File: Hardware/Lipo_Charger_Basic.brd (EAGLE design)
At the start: 29.2 x 10.2 mm, 14 parts, among them U1 MCP73831, X1 Micro USB

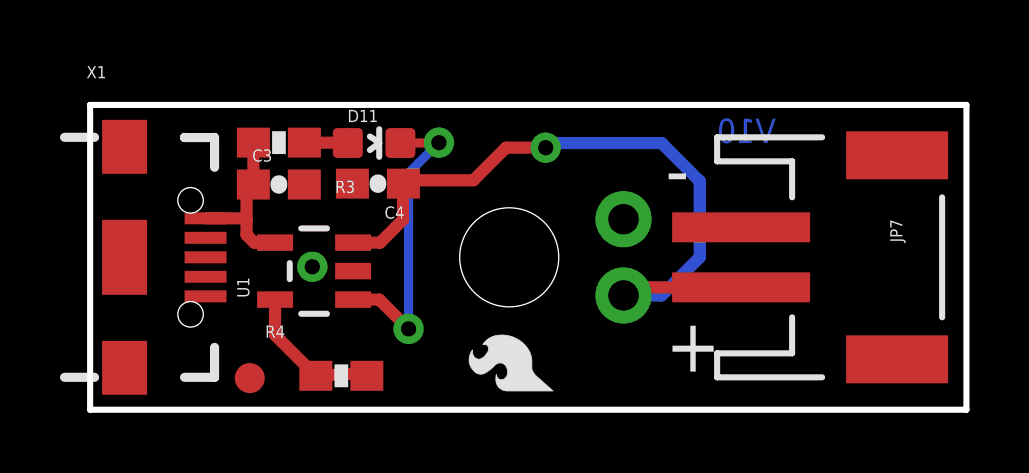
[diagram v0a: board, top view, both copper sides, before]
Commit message: Fixed sch and moved micro B
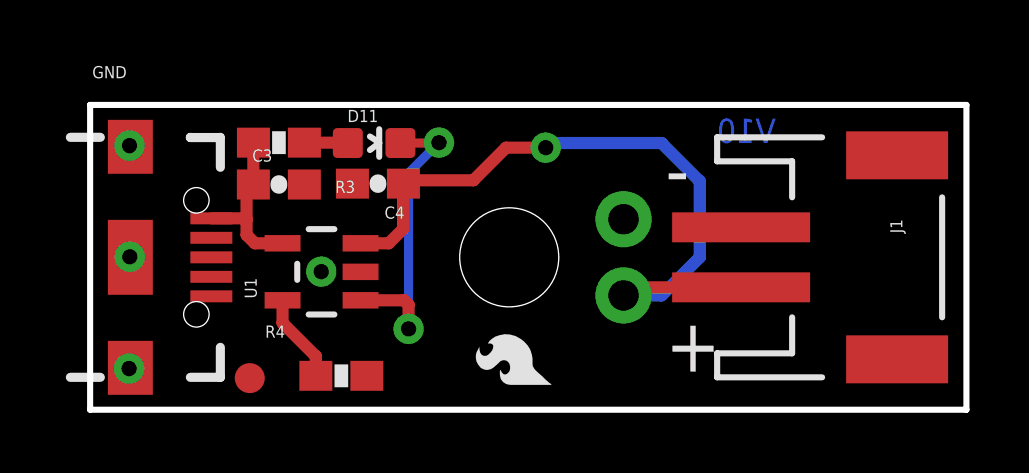
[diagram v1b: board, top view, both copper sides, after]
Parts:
- removed JP1: LOGO-SFESK, SparkFun:SFE-LOGO-FLAME
- removed JP7: LiPo Battery, SparkFun:JST-2-SMD
- removed X1: Micro USB, SparkFun-Connectors:USB-AB-MICRO-SMD_V03
- added GND: Micro USB, SparkFun-Connectors:USB-AB-MICRO-SMD_V03
- added J1: (no value), SparkFun-Connectors:JST-2-SMD
- added LOGO2: SFE_LOGO_FLAME.1_INCH, SparkFun-Aesthetics:SFE_LOGO_FLAME_.1
- JP8: value (none) -> M02PTH; device SparkFun:1X02 -> SparkFun-Connectors:1X02
- moved FRAME1 9.25 mm to (-13.4, -11.4)
- moved U1 0.25 mm to (7.71, 4.60)
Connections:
- net GND: now also GND.GND1, J1.1; no longer JP7.1, X1.GND1
- net VCC: now also J1.2; no longer JP7.2
- net VIN: now also GND.VBUS1; no longer X1.VBUS1
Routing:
- net PROG: track 4.31 -> 2.98 mm

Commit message: Computer Change update.
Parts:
- added JP4: FIDUCIAL1X2, SparkFun:FIDUCIAL-1X2
- added R1: (no value), SparkFun-Resistors:AXIAL-0.1EZ
- moved R4 5.08 mm to (13.5, 1.26)
- moved LOGO2 2.92 mm to (18.7, 0.51)
- renumbered GND to JP9, J1 to JP1
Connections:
- net GND: now also R1.P$1
- net PROG: now also R1.P$2
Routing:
- net PROG: track 2.98 -> 7.49 mm
- net STAT: track 10.4 -> 8.53 mm
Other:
- board text added: "Revised by:Patrick Alberts"
- board text removed: "Revised by: Patrick Alberts"
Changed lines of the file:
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@@
 <setting verticaltext="up"/>
 </settings>
-<grid distance="0.05" unitdist="inch" unit="inch" style="lines" multiple="1" display="yes" altdistance="0.0001" altunitdist="inch" altunit="inch"/>
+<grid distance="0.05" unitdist="inch" unit="inch" style="lines" multiple="1" display="yes" altdistance="0.005" altunitdist="inch" altunit="inch"/>
 <layers>
 <layer number="1" name="Top" color="4" fill="1" visible="yes" active="yes"/>
@@
 <layer number="45" name="Holes" color="7" fill="1" visible="yes" active="yes"/>
 <layer number="46" name="Milling" color="3" fill="1" visible="no" active="yes"/>
-<layer number="47" name="Measures" color="7" fill="1" visible="no" active="yes"/>
+<layer number="47" name="Measures" color="7" fill="1" visible="yes" active="yes"/>
 <layer number="48" name="Document" color="7" fill="1" visible="no" active="yes"/>
-<layer number="49" name="Reference" color="7" fill="1" visible="yes" active="yes"/>
+<layer number="49" name="Reference" color="7" fill="1" visible="no" active="yes"/>
 <layer number="50" name="dxf" color="7" fill="1" visible="no" active="yes"/>
 <layer number="51" name="tDocu" color="6" fill="1" visible="yes" active="yes"/>
@@
 <text x="23.622" y="0.635" size="1.016" layer="22" font="vector" ratio="15" rot="MR0">LiPo Charger Basic</text>
 <text x="22.86" y="8.89" size="0.8128" layer="16" font="vector" ratio="15" rot="MR0">V10</text>
-<text x="17.78" y="-11.43" size="1.778" layer="51" font="vector" ratio="10">N. Seidle</text>
-<text x="-1.93548125" y="-14.378940625" size="1.778" layer="51" font="vector" ratio="10">Revised by: Patrick Alberts</text>
+<text x="16.637" y="-11.43" size="1.778" layer="51" font="vector" ratio="10">N. Seidle</text>
+<text x="-1.93548125" y="-14.378940625" size="1.778" layer="51" font="vector" ratio="10">Revised by:Patrick Alberts</text>
 <dimension x1="-7.62" y1="0" x2="-7.62" y2="10.16" x3="-10.16" y3="5.08" textsize="1.778" textratio="15" layer="47"/>
 <dimension x1="0" y1="15.24" x2="29.21" y2="15.24" x3="14.605" y3="16.51" textsize="1.778" textratio="15" layer="47"/>
@@
 </element>
 <element name="U1" library="SparkFun" package="SOT23-5" value="MCP73831" x="7.713984375" y="4.5974" rot="R90"/>
-<element name="R4" library="SparkFun-Resistors" package="0603-RES" value="2.0k" x="8.374384375" y="1.130303125" smashed="yes">
-<attribute name="NAME" x="5.834384375" y="2.400303125" size="0.4064" layer="25" font="vector"/>
-<attribute name="PROD_ID" value="RES-08296" x="8.374384375" y="1.130303125" size="1.778" layer="27" display="off"/>
-<attribute name="VALUE" value="2.0k" x="8.374384375" y="1.130303125" size="1.778" layer="27" display="off"/>
+<element name="R4" library="SparkFun-Resistors" package="0603-RES" value="2.0k" x="13.454384375" y="1.257303125" smashed="yes">
+<attribute name="NAME" x="10.914384375" y="2.527303125" size="0.4064" layer="25" font="vector"/>
+<attribute name="PROD_ID" value="RES-08296" x="13.454384375" y="1.257303125" size="1.778" layer="27" display="off"/>
+<attribute name="VALUE" value="2.0k" x="13.454384375" y="1.257303125" size="1.778" layer="27" display="off"/>
 </element>
 <element name="JP2" library="SparkFun" package="STAND-OFF" value="STAND-OFF" x="13.97" y="5.08"/>
@@
 </element>
 <element name="JP8" library="SparkFun-Connectors" package="1X02" value="M02PTH" x="17.78" y="6.35" rot="MR270"/>
-<element name="GND" library="SparkFun-Connectors" package="USB-AB-MICRO-SMD_V03" value="Micro USB" x="1.341121875" y="5.08">
+<element name="JP9" library="SparkFun-Connectors" package="USB-AB-MICRO-SMD_V03" value="Micro USB" x="1.341121875" y="5.08">
 <attribute name="PROD_ID" value="CONN-11794" x="1.341121875" y="5.08" size="1.778" layer="27" display="off"/>
 </element>
@@
 <element name="FRAME1" library="SparkFun-Aesthetics" package="CREATIVE_COMMONS" value="FRAME-LETTER" x="-13.442121875" y="-11.43"/>
 <element name="LOGO1" library="SparkFun-Aesthetics" package="OSHW-LOGO-S" value="OSHW-LOGOS" x="26.67" y="5.08" rot="MR90"/>
-<element name="LOGO2" library="SparkFun-Aesthetics" package="SFE_LOGO_FLAME_.1" value="SFE_LOGO_FLAME.1_INCH" x="15.748" y="0.508" rot="R90"/>
-<element name="J1" library="SparkFun-Connectors" package="JST-2-SMD" value="" x="25.4" y="5.08" rot="R270">
+<element name="LOGO2" library="SparkFun-Aesthetics" package="SFE_LOGO_FLAME_.1" value="SFE_LOGO_FLAME.1_INCH" x="18.669" y="0.508" rot="R90"/>
+<element name="JP1" library="SparkFun-Connectors" package="JST-2-SMD" value="" x="25.4" y="5.08" rot="R270">
 <attribute name="PROD_ID" value="CONN-08352" x="25.4" y="5.08" size="1.778" layer="27" font="vector" ratio="15" rot="R270" display="off"/>
 </element>
+<element name="JP4" library="SparkFun" package="FIDUCIAL-1X2" value="FIDUCIAL1X2" x="19.05" y="8.89"/>
+<element name="R1" library="SparkFun-Resistors" package="AXIAL-0.1EZ" value="" x="7.62" y="1.27"/>
 </elements>
 <signals>
@@
 <contactref element="C3" pad="2"/>
 <contactref element="C4" pad="2"/>
-<contactref element="GND" pad="GND1"/>
+<contactref element="JP9" pad="GND1"/>
 <contactref element="JP8" pad="1"/>
 <via x="7.703815625" y="4.60248125" extent="1-16" drill="0.508"/>
@@
 <via x="1.3233375" y="5.097778125" extent="1-16" drill="0.508"/>
 <via x="1.297934375" y="1.3716" extent="1-16" drill="0.508"/>
-<contactref element="J1" pad="1"/>
+<contactref element="JP1" pad="1"/>
+<contactref element="R1" pad="P$1"/>
 </signal>
 <signal name="VCC">
@@
 <wire x1="13.86331875" y1="8.735059375" x2="15.186659375" y2="8.735059375" width="0.4064" layer="1"/>
 <wire x1="15.3416" y1="8.89" x2="15.186659375" y2="8.735059375" width="0.4064" layer="16"/>
-<contactref element="J1" pad="2"/>
+<contactref element="JP1" pad="2"/>
 <wire x1="21.7" y1="4.08" x2="18.05" y2="4.08" width="0.4064" layer="1"/>
 <wire x1="18.05" y1="4.08" x2="17.78" y2="3.81" width="0.4064" layer="1"/>
@@
 <contactref element="U1" pad="5"/>
 <contactref element="R4" pad="1"/>
-<wire x1="6.413884375" y1="3.6474" x2="6.413884375" y2="2.892675" width="0.4064" layer="1"/>
-<wire x1="7.524384375" y1="1.130303125" x2="7.524384375" y2="1.782175" width="0.4064" layer="1"/>
-<wire x1="7.524384375" y1="1.782175" x2="6.413884375" y2="2.892675" width="0.4064" layer="1"/>
+<contactref element="R1" pad="P$2"/>
+<wire x1="6.413884375" y1="3.6474" x2="6.413884375" y2="3.111115625" width="0.4064" layer="1"/>
+<wire x1="6.413884375" y1="3.111115625" x2="6.858" y2="2.667" width="0.4064" layer="1"/>
+<wire x1="6.858" y1="2.667" x2="8.763" y2="2.667" width="0.4064" layer="1"/>
+<wire x1="8.763" y1="2.667" x2="10.16" y2="1.27" width="0.4064" layer="1"/>
+<wire x1="12.5916875" y1="1.27" x2="10.16" y2="1.27" width="0.4064" layer="1"/>
+<wire x1="12.5916875" y1="1.27" x2="12.604384375" y2="1.257303125" width="0.4064" layer="1"/>
 </signal>
 <signal name="STAT">
@@
 <contactref element="U1" pad="1"/>
 <via x="11.628121875" y="8.9027" extent="1-16" drill="0.508"/>
-<via x="10.614659375" y="2.6949375" extent="1-16" drill="0.508"/>
-<wire x1="10.614659375" y1="2.6949375" x2="10.614659375" y2="7.8892375" width="0.3048" layer="16"/>
-<wire x1="10.614659375" y1="7.8892375" x2="11.628121875" y2="8.9027" width="0.3048" layer="16"/>
-<wire x1="10.34358125" y1="8.89" x2="11.615421875" y2="8.89" width="0.3048" layer="1"/>
+<via x="10.614659375" y="3.7109375" extent="1-16" drill="0.508"/>
+<wire x1="10.614659375" y1="3.7109375" x2="10.614659375" y2="7.8892375" width="0.4064" layer="16"/>
+<wire x1="10.614659375" y1="7.8892375" x2="11.628121875" y2="8.9027" width="0.4064" layer="16"/>
+<wire x1="10.34358125" y1="8.89" x2="11.615421875" y2="8.89" width="0.4064" layer="1"/>
 <wire x1="11.615421875" y1="8.89" x2="11.628121875" y2="8.9027" width="0.3048" layer="1"/>
-<wire x1="9.014084375" y1="3.6474" x2="10.472459375" y2="3.6474" width="0.4064" layer="1"/>
-<wire x1="10.472459375" y1="3.6474" x2="10.614659375" y2="3.5052" width="0.4064" layer="1"/>
-<wire x1="10.614659375" y1="3.5052" x2="10.614659375" y2="2.6949375" width="0.4064" layer="1"/>
+<wire x1="9.014084375" y1="3.6474" x2="10.551121875" y2="3.6474" width="0.4064" layer="1"/>
+<wire x1="10.551121875" y1="3.6474" x2="10.614659375" y2="3.7109375" width="0.4064" layer="1"/>
 </signal>
 <signal name="VIN">
@@
 <contactref element="U1" pad="4"/>
 <contactref element="C3" pad="1"/>
-<contactref element="GND" pad="VBUS1"/>
+<contactref element="JP9" pad="VBUS1"/>
 <wire x1="5.44158125" y1="7.508240625" x2="5.44158125" y2="8.900159375" width="0.4064" layer="1"/>
 <wire x1="5.44158125" y1="8.900159375" x2="5.444121875" y2="8.9027" width="0.4064" layer="1"/>

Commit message: qc checklist issues fixed.
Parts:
- JP1: value (none) -> JST
- U1: device SparkFun:SOT23-5 -> SparkFun-PowerIC:SOT23-5
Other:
- board text added: "V01"
- board text removed: "V10"
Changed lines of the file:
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@@
 <layer number="45" name="Holes" color="7" fill="1" visible="yes" active="yes"/>
 <layer number="46" name="Milling" color="3" fill="1" visible="no" active="yes"/>
-<layer number="47" name="Measures" color="7" fill="1" visible="yes" active="yes"/>
+<layer number="47" name="Measures" color="7" fill="1" visible="no" active="yes"/>
 <layer number="48" name="Document" color="7" fill="1" visible="no" active="yes"/>
 <layer number="49" name="Reference" color="7" fill="1" visible="no" active="yes"/>
@@
 <layer number="251" name="SMDround" color="12" fill="11" visible="no" active="no"/>
 <layer number="254" name="cooling" color="7" fill="1" visible="no" active="yes"/>
+<layer number="255" name="routoute" color="7" fill="1" visible="yes" active="yes"/>
 </layers>
 <board>
@@
 <text x="20.955" y="2.921" size="1.778" layer="22" font="vector" ratio="15" rot="MR0">+</text>
 <text x="23.622" y="0.635" size="1.016" layer="22" font="vector" ratio="15" rot="MR0">LiPo Charger Basic</text>
-<text x="22.86" y="8.89" size="0.8128" layer="16" font="vector" ratio="15" rot="MR0">V10</text>
+<text x="22.86" y="8.89" size="0.8128" layer="16" font="vector" ratio="15" rot="MR0">V01</text>
 <text x="16.637" y="-11.43" size="1.778" layer="51" font="vector" ratio="10">N. Seidle</text>
 <text x="-1.93548125" y="-14.378940625" size="1.778" layer="51" font="vector" ratio="10">Revised by:Patrick Alberts</text>
@@
 <attribute name="VALUE" value="330" x="6.294121875" y="8.9027" size="1.778" layer="27" rot="R180" display="off"/>
 </element>
-<element name="U1" library="SparkFun" package="SOT23-5" value="MCP73831" x="7.713984375" y="4.5974" rot="R90"/>
+<element name="U1" library="SparkFun-PowerIC" package="SOT23-5" value="MCP73831" x="7.713984375" y="4.5974" rot="R90">
+<attribute name="PROD_ID" value="IC-09995" x="7.713984375" y="4.5974" size="1.778" layer="27" rot="R90" display="off"/>
+</element>
 <element name="R4" library="SparkFun-Resistors" package="0603-RES" value="2.0k" x="13.454384375" y="1.257303125" smashed="yes">
 <attribute name="NAME" x="10.914384375" y="2.527303125" size="0.4064" layer="25" font="vector"/>
@@
 <element name="LOGO1" library="SparkFun-Aesthetics" package="OSHW-LOGO-S" value="OSHW-LOGOS" x="26.67" y="5.08" rot="MR90"/>
 <element name="LOGO2" library="SparkFun-Aesthetics" package="SFE_LOGO_FLAME_.1" value="SFE_LOGO_FLAME.1_INCH" x="18.669" y="0.508" rot="R90"/>
-<element name="JP1" library="SparkFun-Connectors" package="JST-2-SMD" value="" x="25.4" y="5.08" rot="R270">
+<element name="JP1" library="SparkFun-Connectors" package="JST-2-SMD" value="JST" x="25.4" y="5.08" rot="R270">
 <attribute name="PROD_ID" value="CONN-08352" x="25.4" y="5.08" size="1.778" layer="27" font="vector" ratio="15" rot="R270" display="off"/>
 </element>
@@
 </signal>
 </signals>
-<errors>
-</errors>
 </board>
 </drawing>
